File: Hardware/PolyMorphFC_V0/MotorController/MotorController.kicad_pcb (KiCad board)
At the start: 2 copper layers, 78 parts, among them J1 Conn_01x03_Pin, J3 Conn_01x02_Pin, J5 JST_XH_01x06, J6 Conn_01x02_Pin, Q1 BSC016N06NS, Q2 BSC016N06NS, Q3 BSC016N06NS, Q4 BSC016N06NS, Q5 BSC016N06NS, Q6 BSC016N06NS, SW1 SW_Push, U1 STSPIN32G4, U5 AS5048A

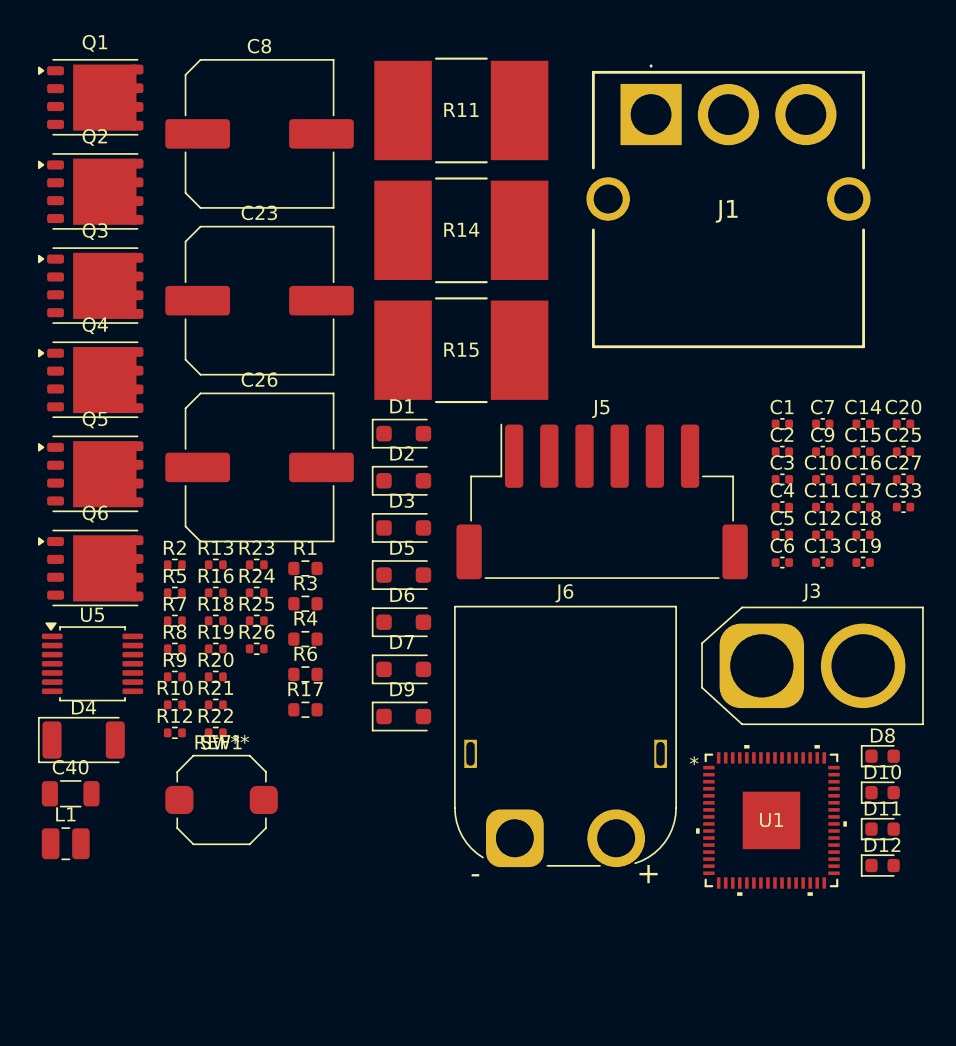
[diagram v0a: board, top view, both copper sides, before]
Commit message: Footprint placements and screens
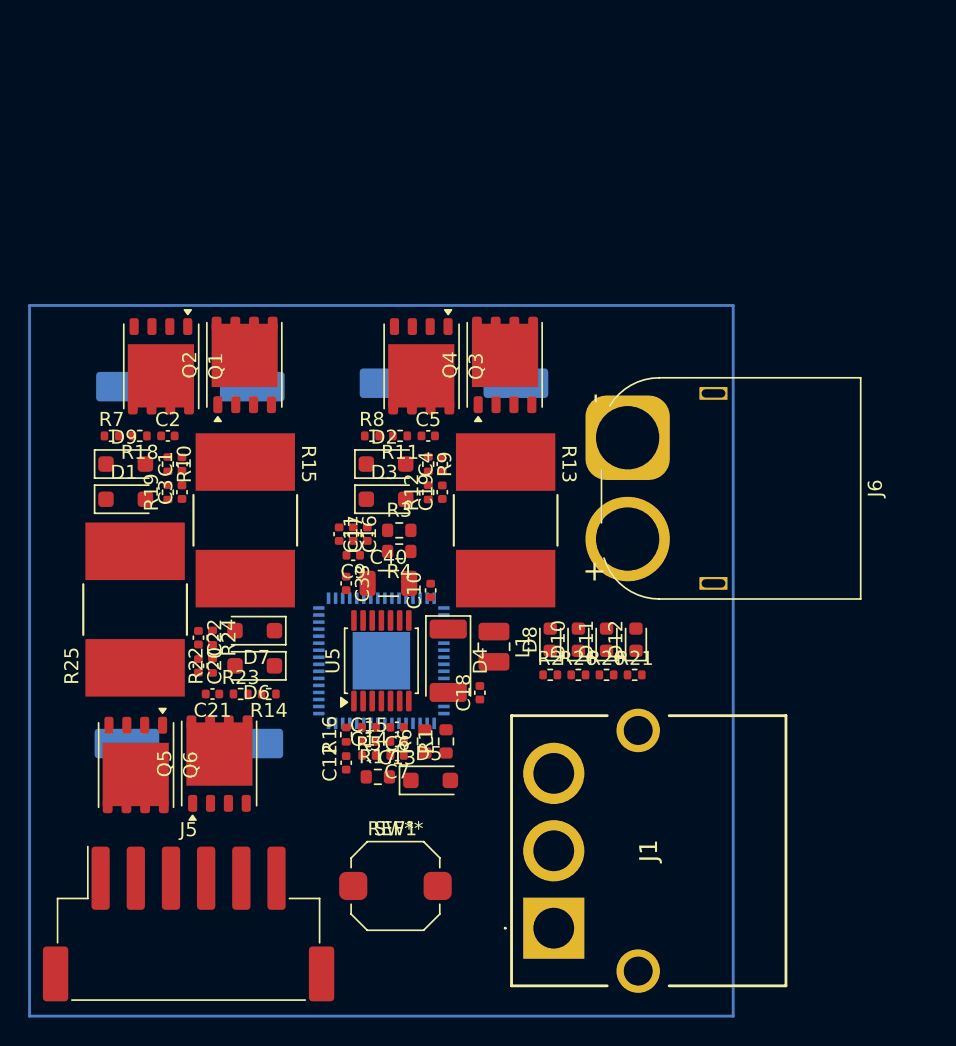
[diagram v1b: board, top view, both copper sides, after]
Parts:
- removed C25, C27: 1uF, Capacitor_SMD:C_0402_1005Metric
- added C21: 1uF, Capacitor_SMD:C_0402_1005Metric, F.Cu at (108.5, 96.9)
- added C22: 1uF, Capacitor_SMD:C_0402_1005Metric, F.Cu at (107.5, 92.9)
- C23, C26, C8, J3, U1: moved to B.Cu
- R11: value 5mΩ -> 10Ω; footprint Resistor_SMD:R_4527_11375MetricL -> Resistor_SMD:R_0402_1005Metric
- R12: value 15Ω -> 10Ω
- R13: value 15Ω -> 5mΩ; footprint Resistor_SMD:R_0402_1005Metric -> Resistor_SMD:R_4527_11375MetricL
- R14: value 5mΩ -> 15Ω; footprint Resistor_SMD:R_4527_11375MetricL -> Resistor_SMD:R_0402_1005Metric
- R22: value 10Ω -> 15Ω
- R25: value 10Ω -> 5mΩ; footprint Resistor_SMD:R_0402_1005Metric -> Resistor_SMD:R_4527_11375MetricL
- moved J1 58.2 mm to (132.8, 113.5), turned to 90 degrees
- moved C20 53.0 mm to (107.5, 94.9), turned to -90 degrees
- moved C2 43.7 mm to (105.3, 78.5)
- moved C1 42.8 mm to (106.3, 80.5), turned to 90 degrees
- moved C3 42.7 mm to (106.3, 82.5), turned to 90 degrees
- moved C14 42.3 mm to (119.6, 101.2)
- moved J5 42.0 mm to (106.8, 113.2)
- moved C15 40.7 mm to (119.6, 100.2)
- moved C33 40.0 mm to (118.0, 89.0), turned to -90 degrees
- moved C7 38.3 mm to (121.6, 101.2), turned to 180 degrees
- moved C12 37.5 mm to (118.0, 101.8), turned to 90 degrees
- moved C17 37.3 mm to (117.5, 85.5), turned to -90 degrees
- moved C16 36.4 mm to (118.5, 85.5), turned to -90 degrees
- moved R14 35.7 mm to (112.5, 96.9), turned to 180 degrees
- moved C9 34.2 mm to (118.5, 87.0), turned to 180 degrees
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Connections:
- J1 pad 1: /OUT1 -> /PHASE_A
- J1 pad 2: /OUT2 -> /PHASE_B
- J1 pad 3: /OUT3 -> /PHASE_C
- R11 pad 1: /Shunt_H2 -> Net-(D2-A)
- R11 pad 2: GND -> Net-(Q3-G)
- R12 pad 1: /GHS3 -> Net-(D3-A)
- R12 pad 2: Net-(Q5-G) -> Net-(Q4-G)
- R13 pad 1: /GLS3 -> /Shunt_H2
- R13 pad 2: Net-(Q6-G) -> GND
- R14 pad 1: /Shunt_H3 -> /GHS3
- R14 pad 2: GND -> Net-(Q5-G)
- R22 pad 1: Net-(D2-A) -> /GLS3
- R22 pad 2: Net-(Q3-G) -> Net-(Q6-G)
- R23 pad 1: Net-(D3-A) -> Net-(D6-A)
- R23 pad 2: Net-(Q4-G) -> Net-(Q5-G)
- R24 pad 1: Net-(D6-A) -> Net-(D7-A)
- R24 pad 2: Net-(Q5-G) -> Net-(Q6-G)
- R25 pad 1: Net-(D7-A) -> /Shunt_H3
- R25 pad 2: Net-(Q6-G) -> GND
